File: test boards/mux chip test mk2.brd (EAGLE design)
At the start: 49.8 x 19 mm, 39 parts, among them IC1 741G3157DRLR, IC2 74AHC1G125DBV, IC3 741G3157DRLR, SW1 SPST_TACT-KMR2, U1 ATMEGA168MLF, Y1 16MHZ

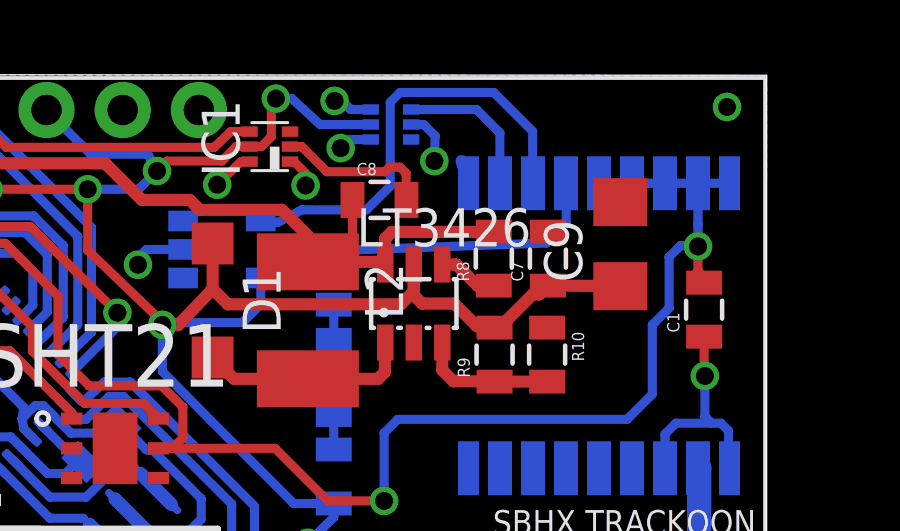
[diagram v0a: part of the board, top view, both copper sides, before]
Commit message: Moved mix test LED
changed the schematic on the mux test to move the pulse per second LED
to the correct area on the schematic.
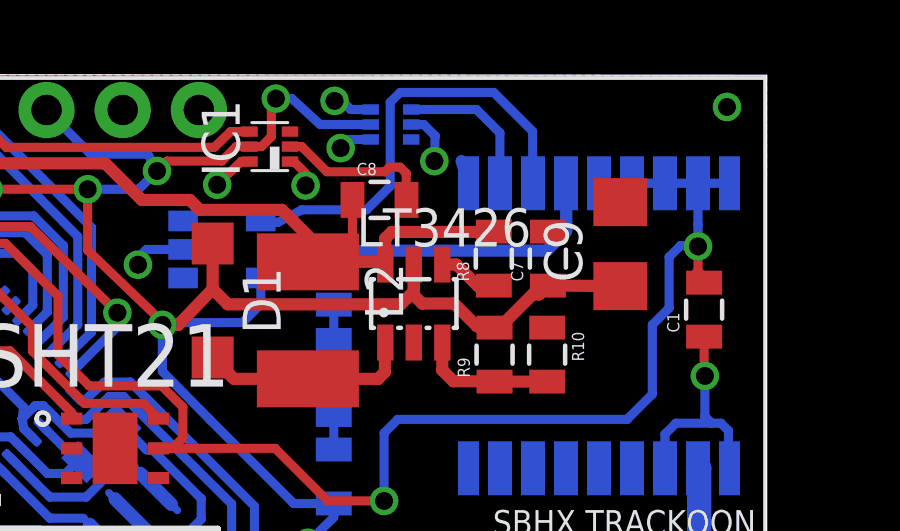
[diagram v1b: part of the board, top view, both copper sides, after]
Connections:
- net N$2 renamed PPS
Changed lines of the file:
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@@
 <grid distance="0.001" unitdist="inch" unit="inch" style="lines" multiple="1" display="no" altdistance="0.025" altunitdist="inch" altunit="inch"/>
 <layers>
-<layer number="1" name="Top" color="4" fill="1" visible="no" active="yes"/>
+<layer number="1" name="Top" color="4" fill="1" visible="yes" active="yes"/>
 <layer number="2" name="Route2" color="1" fill="3" visible="yes" active="yes"/>
 <layer number="3" name="Route3" color="4" fill="3" visible="no" active="no"/>
 <layer number="14" name="Route14" color="1" fill="6" visible="no" active="no"/>
 <layer number="15" name="Route15" color="4" fill="6" visible="yes" active="yes"/>
-<layer number="16" name="Bottom" color="1" fill="1" visible="no" active="yes"/>
+<layer number="16" name="Bottom" color="1" fill="1" visible="yes" active="yes"/>
 <layer number="17" name="Pads" color="2" fill="1" visible="yes" active="yes"/>
 <layer number="18" name="Vias" color="2" fill="1" visible="yes" active="yes"/>
@@
 <wire x1="21.64271875" y1="5.94551875" x2="22.256059375" y2="5.94551875" width="0.3048" layer="16"/>
 </signal>
-<signal name="N$2">
-<contactref element="U$1" pad="4_TIMEPULSE"/>
-<contactref element="R1" pad="1"/>
-<wire x1="28.9052" y1="13.1682" x2="36.0028" y2="13.4222" width="0.3048" layer="16"/>
-<wire x1="36.0028" y1="13.4222" x2="36.6522" y2="14.0716" width="0.3048" layer="16"/>
-<wire x1="36.6522" y1="14.0716" x2="36.6522" y2="15.5094" width="0.3048" layer="16"/>
-<wire x1="36.6522" y1="15.5094" x2="36.6452" y2="15.4148" width="0.3048" layer="16"/>
-</signal>
 <signal name="N$4">
 </signal>
@@
 <wire x1="22.6568" y1="13.208" x2="23.8814" y2="13.208" width="0.3048" layer="16"/>
 </signal>
+<signal name="PPS">
+<contactref element="R1" pad="1"/>
+<contactref element="U$1" pad="4_TIMEPULSE"/>
+<wire x1="28.9052" y1="13.1682" x2="36.0028" y2="13.1682" width="0.4064" layer="16"/>
+<wire x1="36.0028" y1="13.1682" x2="36.6522" y2="13.8176" width="0.4064" layer="16"/>
+<wire x1="36.6522" y1="13.8176" x2="36.6522" y2="15.4078" width="0.4064" layer="16"/>
+<wire x1="36.6522" y1="15.4078" x2="36.6452" y2="15.4148" width="0.4064" layer="16"/>
+</signal>
 </signals>
